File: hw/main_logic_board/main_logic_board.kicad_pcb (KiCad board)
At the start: 4 copper layers, 61.9 x 69 mm, 115 parts, among them J1 BATT_IN, J11 SPI1, J12 UART0, J13 UART2, J14 UART4, J15 I2C1, J16 I2C2, J17 5V, J18 3V3, J19 BATT_V, J2 5V_PWR_SEL, J3 3V3_PWR_SEL, J4 USB_A, J5 RC_OUT_1, J6 RC_OUT_2, J7 RC_OUT_3, J8 RC_OUT_4, SW1 ESP_RESET, SW2 ESP_GPIO0, U1 PocketBeagle, U10 ICM-20948, U11 VL53L1X, U12 ACS725xLCTR-40AB, U2 74LVC2T45DC, U3 BME280, U4 NCP1117-5.0_SOT223, U5 NCP1117-3.3_SOT223, U6 TPS563200, U7 TPS563200, U8 ESP-12F, U9 USBLC6-2P6

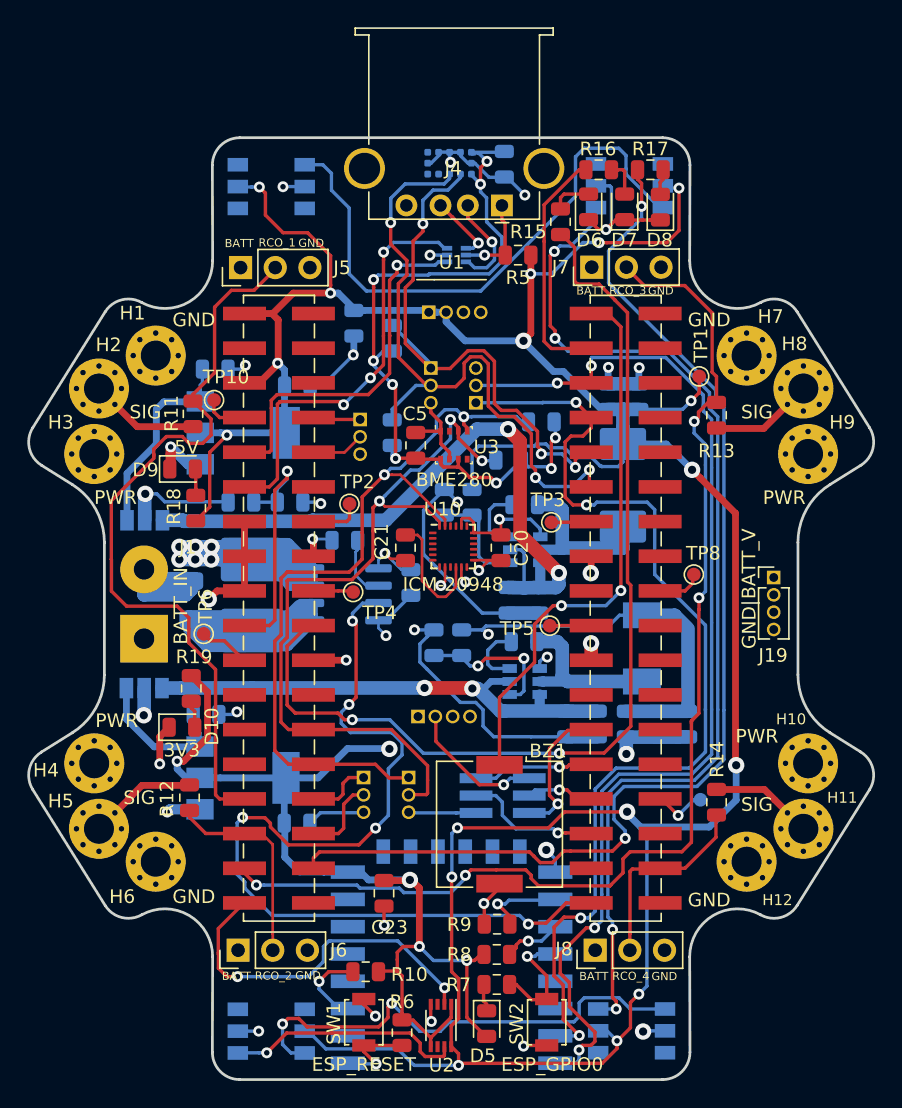
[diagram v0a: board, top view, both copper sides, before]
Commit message: Some more slight silk adjustments + naming
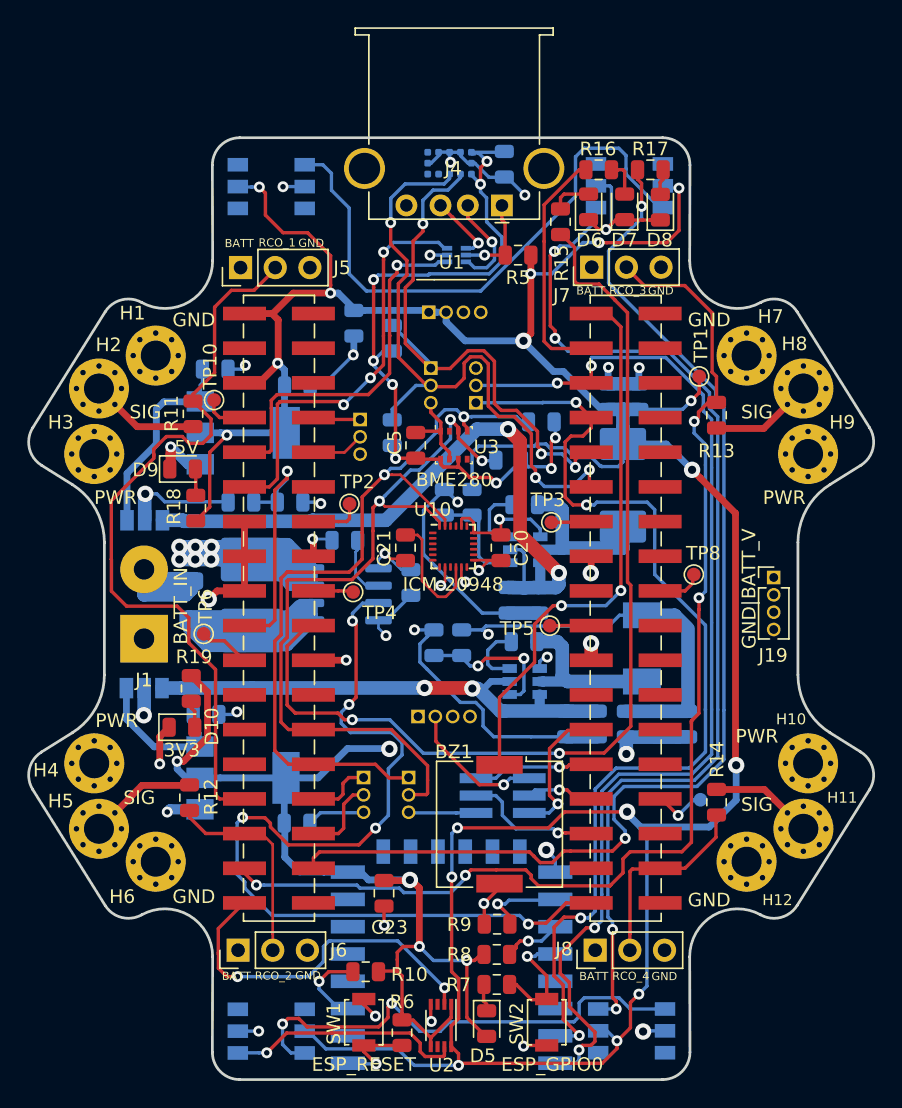
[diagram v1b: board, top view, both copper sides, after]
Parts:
- added G1: LOGO, lib:drone_icon, B.Cu at (168.7, 86.7)
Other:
- board text added: "Micro Drone MLB Version 1 By Krisztian K. and Utkarsh S."
